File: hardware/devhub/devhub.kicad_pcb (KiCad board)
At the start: 4 copper layers, 100 x 100 mm, 156 parts, among them J1 USB-C PWR IN, J101 USB-C, J2 USB-C UPSTREAM, J201 USB-C, J301 USB-C, J4 SWD, J401 USB-C, J5 Banana COM 1, J6 Banana NC 1, J9 UART debug, K1 G5Q-1 DC5, SW1 relè on/off, SW101 porta on/off, SW201 porta on/off, SW301 porta on/off, SW401 porta on/off, U1 AP7361C-33ER, U101 PI3USB4002A, U12 MCP120T-300I/TT, U13 TPS259470ARPWR, U2 USB2517I-JZX, U201 PI3USB4002A, U3 STM32G0B1CEU6, U301 PI3USB4002A, U4 UCS2114-1-V/LX, U401 PI3USB4002A, U5 UCS2114-1-V/LX, U9 ULN2003V12, Y1 24MHz 12pF

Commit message: Test points, LED host moved, board finished (D92)
- 14 test points: GND loops TP1/TP10 (Keystone 5001), pads for +5V, +3V3,
  I2C1/I2C2, HUB_RST_N, EFUSE_FLT_N and VBUS_P1-P4
- D93/R93 moved to the rear, left of J1
- Button symbols: generic Value, function in Description; PCB aligned
- Docs: decision D92, components, PCB test rules, LED host position
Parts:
- added TP1: Keystone 5001, TestPoint:TestPoint_Keystone_5000-5004_Miniature, B.Cu at (119.4, 50.2)
- added TP10: Keystone 5001, TestPoint:TestPoint_Keystone_5000-5004_Miniature, B.Cu at (90.4, 99.7)
- added TP11: VBUS_P1, TestPoint:TestPoint_Pad_D1.5mm, B.Cu at (156.8, 128.8)
- added TP12: VBUS_P2, TestPoint:TestPoint_Pad_D1.5mm, B.Cu at (139.1, 121.1)
- added TP13: VBUS_P3, TestPoint:TestPoint_Pad_D1.5mm, B.Cu at (126.8, 128.8)
- added TP14: VBUS_P4, TestPoint:TestPoint_Pad_D1.5mm, B.Cu at (109.2, 121.1)
- added TP2: +5V, TestPoint:TestPoint_Pad_D1.5mm, B.Cu at (119.4, 53.3)
- added TP3: +3V3, TestPoint:TestPoint_Pad_D1.5mm, B.Cu at (119.4, 55.9)
- added TP4: I2C1_SCL, TestPoint:TestPoint_Pad_D1.5mm, B.Cu at (129.5, 88.2)
- added TP5: I2C1_SDA, TestPoint:TestPoint_Pad_D1.5mm, B.Cu at (106.0, 96.8)
- added TP6: I2C2_SCL, TestPoint:TestPoint_Pad_D1.5mm, B.Cu at (94.1, 85.5)
- added TP7: I2C2_SDA, TestPoint:TestPoint_Pad_D1.5mm, B.Cu at (102.3, 102.7)
- added TP8: HUB_RST_N, TestPoint:TestPoint_Pad_D1.5mm, B.Cu at (118.8, 74.5)
- added TP9: EFUSE_FLT_N, TestPoint:TestPoint_Pad_D1.5mm, B.Cu at (92.0, 77.1)
- SW1: value relè on/off -> Push button switch, generic, two pins
- SW101, SW201, SW301, SW401: value porta on/off -> Push button switch, generic, two pins
- moved D93 23.9 mm to (70.5, 57.5)
- moved R93 19.0 mm to (75.5, 57.5), turned to 180 degrees
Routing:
- net +3V3: track 65.4 -> 74.8 mm
- net +5V: track 230.7 -> 237.5 mm
- net /MCU STM32G0B1/LED_HOST: track 36.7 -> 42.4 mm
- net VBUS_P1: track 29.2 -> 34.9 mm
- net VBUS_P3: track 29.2 -> 34.9 mm
- net I2C2_SCL: track 73.9 -> 72.5 mm
- net I2C1_SDA: track 76.8 -> 77.8 mm
- net I2C2_SDA: track 78.0 -> 77.2 mm
- net GND: track 235.2 -> 234.5 mm
- net HUB_RST_N: track 60.5 -> 59.8 mm
- net EFUSE_FLT_N: vias 2 -> 3

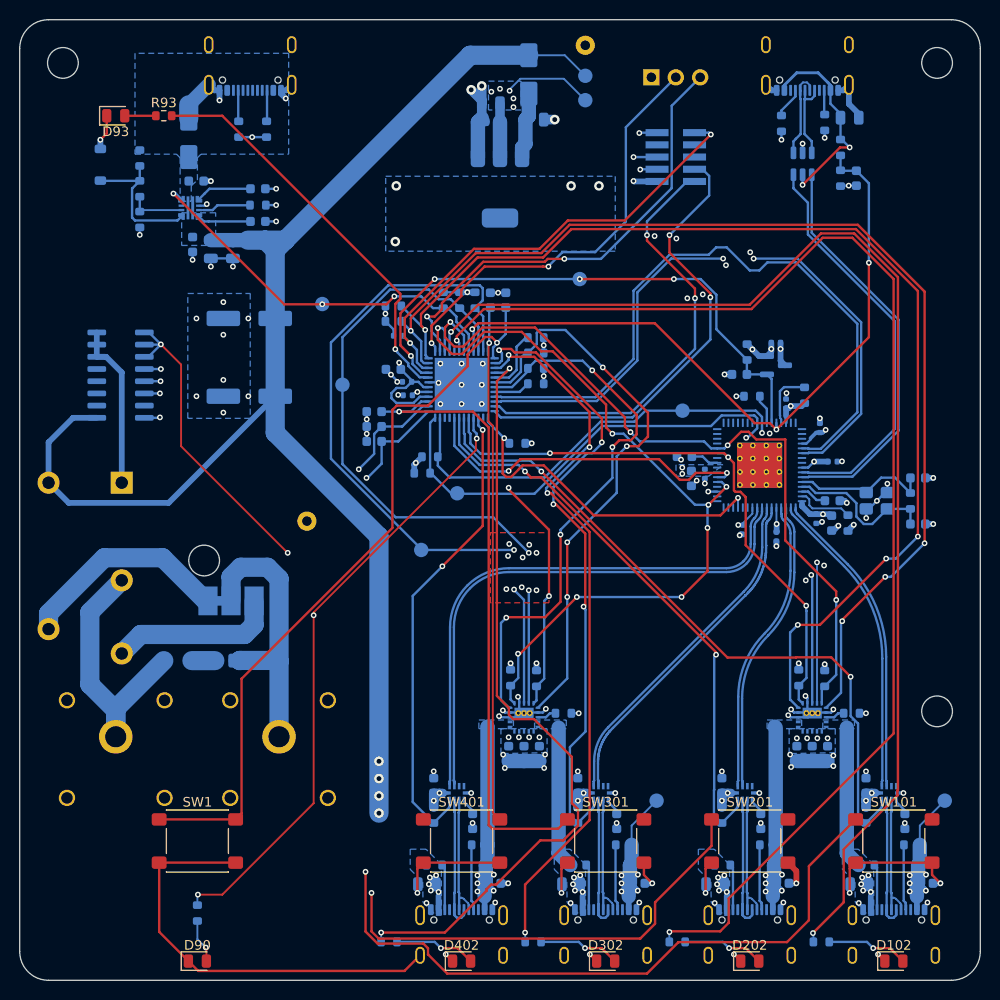
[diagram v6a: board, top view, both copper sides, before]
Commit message: Bigger vias for power and gnd Lines
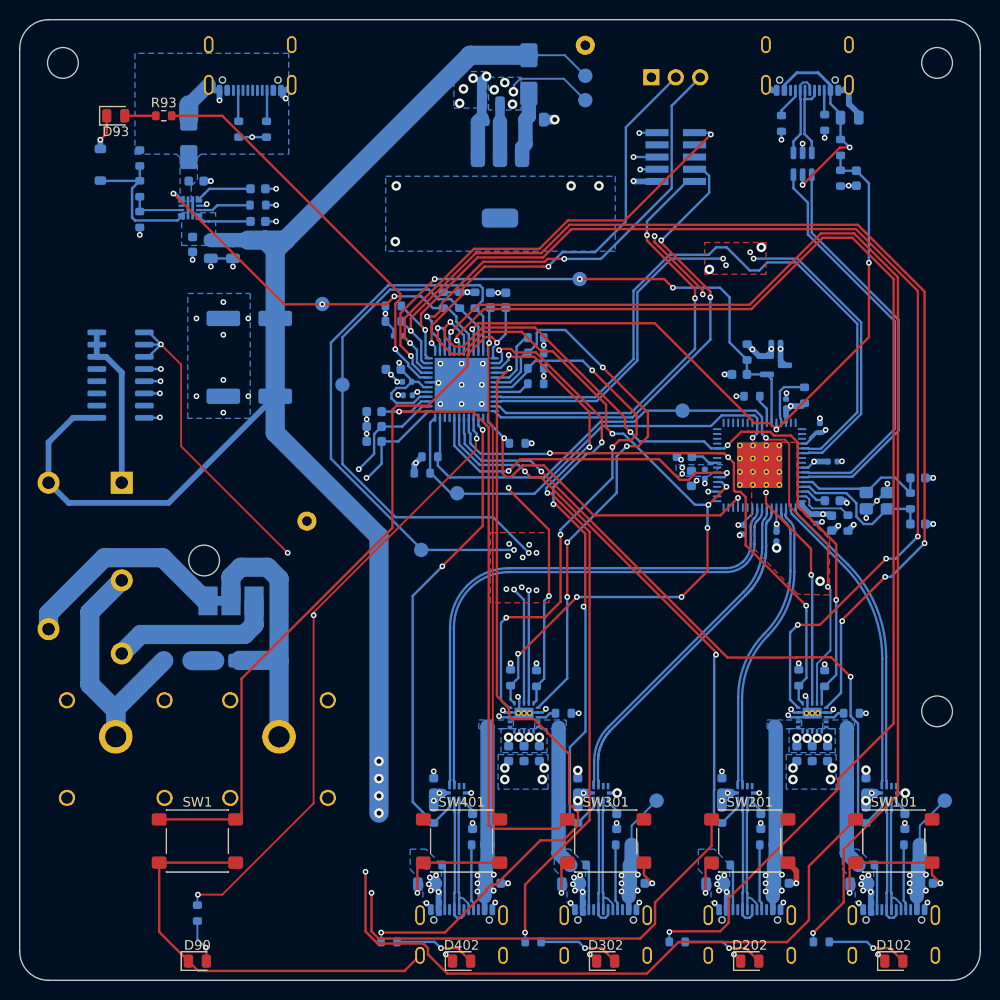
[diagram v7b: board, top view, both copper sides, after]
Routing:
- net I2C1_SCL: track 74.8 -> 76.9 mm
- net GND: track 234.5 -> 233.2 mm
- net I2C1_SDA: track 77.8 -> 77.0 mm, vias 2 -> 3
- net /MCU STM32G0B1/SWCLK: track 48.4 -> 49.2 mm
- net HUB_RST_N: track 59.8 -> 60.5 mm
- net FAULT_P1: track 79.3 -> 79.9 mm
- net +3V3: track 74.8 -> 74.7 mm, vias 37 -> 36

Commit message: +5V copper zones on B.Cu and In1.Cu to lower the U13 to U4/U5 resistance
Replace the 2 mm +5V trunk with a B.Cu zone from U13 and an In1.Cu zone
along the front edge, including the risers to U4 and U5. Simulated DC
resistance from U13 to U4 drops from 48.8 to 13.8 mOhm, to U5 from 32.3
to 9.0 mOhm (41 and 27 mV at 3 A).
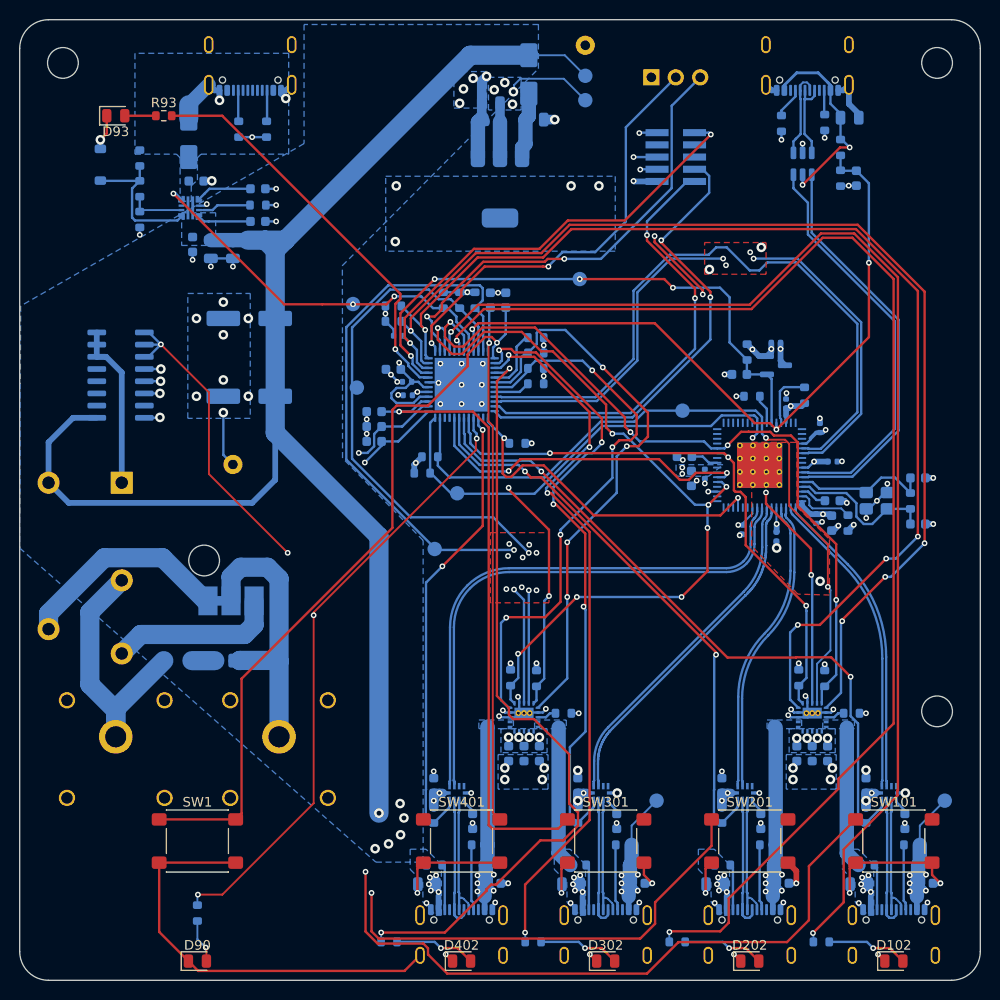
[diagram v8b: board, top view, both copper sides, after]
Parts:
- moved TP10 9.70 mm to (82.7, 93.8)
- moved TP9 3.20 mm to (95.2, 77.1)
- moved TP6 1.53 mm to (95.6, 85.8)
- moved TP7 1.40 mm to (103.7, 102.6)
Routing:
- net GND: track 233.2 -> 239.3 mm
- net I2C2_SDA: track 77.2 -> 75.0 mm
- net I2C2_SCL: track 72.5 -> 70.8 mm
- net OE_N_P4: track 49.5 -> 48.4 mm
- net BTN_P2: track 103.6 -> 104.2 mm
- net +5V: track 237.5 -> 237.2 mm, vias 12 -> 14
- added copper zone on In1.Cu, net +5V
